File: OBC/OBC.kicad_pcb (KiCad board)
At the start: 4 copper layers, 90.3 x 95.8 mm, 53 parts

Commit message: Clean up GND routing to RPCM4 H1/H2 headers
- Removed 45 degree GND traces running to the H1 and H2 header pads
- Replaced long GND traces with short stubs and vias down to the
  GND plane (layer 2)
- Shorter return paths and less top layer clutter around the headers
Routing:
- net GND: track 225.9 -> 143.6 mm, vias 4 -> 8

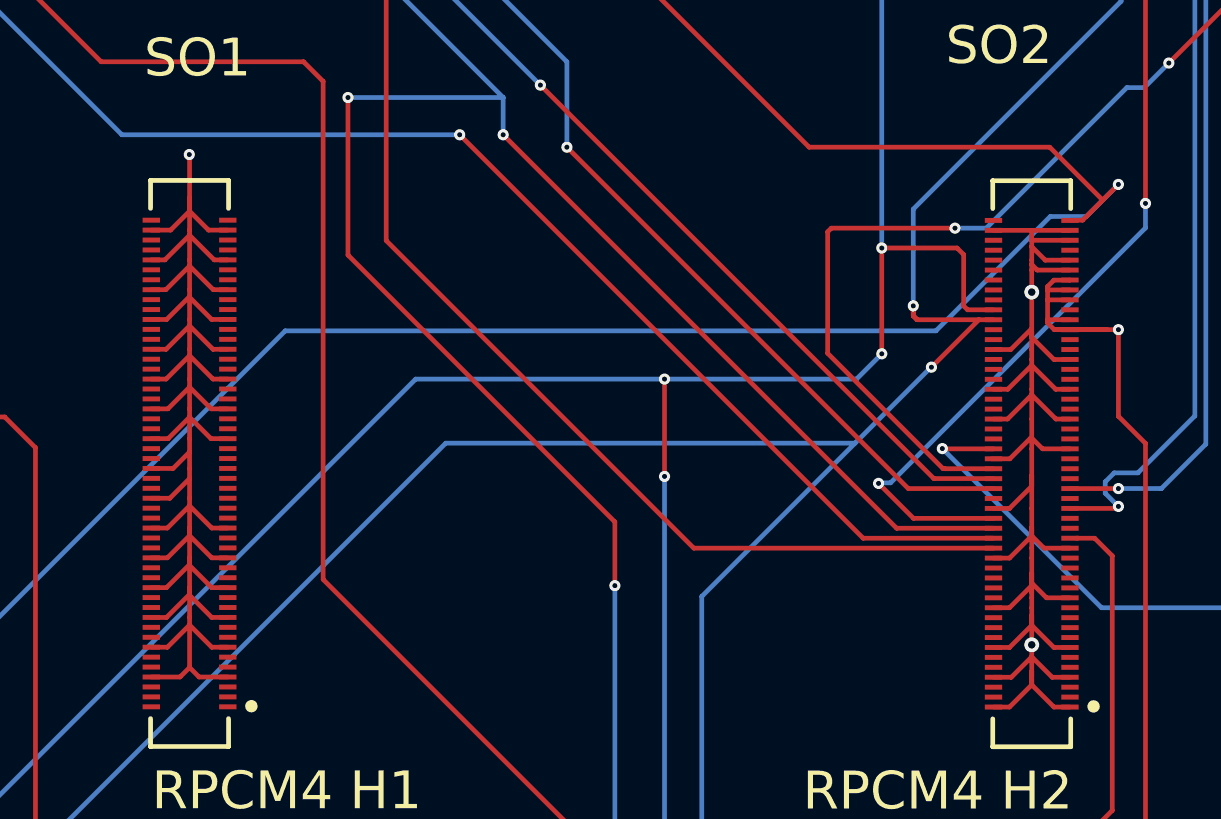
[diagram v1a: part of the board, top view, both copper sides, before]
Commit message: Clean up GND routing on RPCM4 H1 header
- Removed unnecessary long GND traces on H1
- Replaced them with short stubs and vias down to the GND plane
  (layer 2)
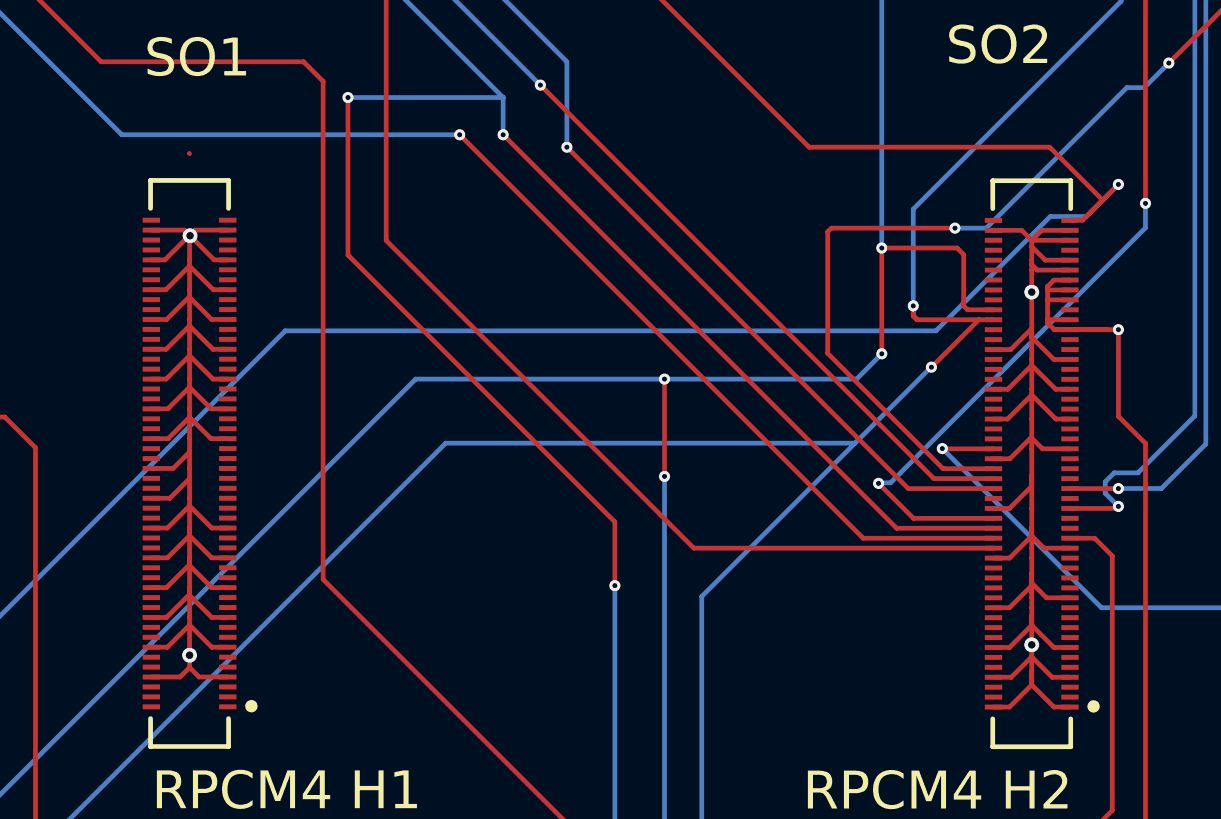
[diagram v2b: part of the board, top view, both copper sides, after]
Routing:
- net GND: track 143.6 -> 139.4 mm, vias 8 -> 9
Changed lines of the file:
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@@
-	)
-	(segment
-		(start 130.51028 89.74366)
-		(end 131.28609 89.74366)
-		(width 0.19)
-		(layer "F.Cu")
-		(net "GND")
 	)
 	(segment
@@
 	)
 	(segment
-		(start 129.74609 88.44947)
-		(end 129.74609 88.82507)
-		(width 0.19)
-		(layer "F.Cu")
-		(net "GND")
-	)
-	(segment
 		(start 164.16011 102.55366)
 		(end 165.20609 102.55366)
@@
 	)
 	(segment
+		(start 164.0661 89.75366)
+		(end 165.20609 89.75366)
+		(width 0.19)
+		(layer "F.Cu")
+		(net "GND")
+	)
+	(segment
 		(start 129.74609 96.06947)
 		(end 129.74609 95.74366)
@@
 	(segment
 		(start 129.74609 89.94947)
-		(end 130.74028 90.94366)
+		(end 129.76679 89.97017)
 		(width 0.19)
 		(layer "F.Cu")
@@
 	)
 	(segment
-		(start 163.6661 90.15366)
-		(end 163.6661 89.75366)
-		(width 0.19)
-		(layer "F.Cu")
-		(net "GND")
-	)
-	(segment
 		(start 163.6661 96.37947)
 		(end 164.64029 97.35366)
@@
 	)
 	(segment
-		(start 129.74609 88.44947)
-		(end 129.74609 86.66427)
-		(width 0.19)
-		(layer "F.Cu")
-		(net "GND")
-	)
-	(segment
 		(start 129.74609 100.84947)
 		(end 128.8519 101.74366)
@@
 	)
 	(segment
+		(start 129.74609 89.94947)
+		(end 129.9519 89.74366)
+		(width 0.19)
+		(layer "F.Cu")
+		(net "GND")
+	)
+	(segment
 		(start 162.69191 97.35366)
 		(end 162.12609 97.35366)
@@
 	)
 	(segment
+		(start 129.74609 89.94947)
+		(end 129.54028 89.74366)
+		(width 0.19)
+		(layer "F.Cu")
+		(net "GND")
+	)
+	(segment
 		(start 129.74609 90.94366)
 		(end 129.74609 89.94947)
@@
 	)
 	(segment
+		(start 163.2661 89.75366)
+		(end 162.12609 89.75366)
+		(width 0.19)
+		(layer "F.Cu")
+		(net "GND")
+	)
+	(segment
 		(start 163.6661 95.18947)
 		(end 163.6661 94.95366)
@@
 	)
 	(segment
-		(start 163.6661 89.75366)
-		(end 162.12609 89.75366)
-		(width 0.19)
-		(layer "F.Cu")
-		(net "GND")
-	)
-	(segment
 		(start 163.6661 93.84947)
 		(end 163.6661 93.70947)
@@
 	)
 	(segment
-		(start 128.9819 89.74366)
-		(end 128.20609 89.74366)
-		(width 0.19)
-		(layer "F.Cu")
-		(net "GND")
-	)
-	(segment
 		(start 129.74609 102.04966)
 		(end 128.85209 102.94366)
@@
 	)
 	(segment
-		(start 129.74609 89.94947)
-		(end 129.74609 89.74366)
-		(width 0.19)
-		(layer "F.Cu")
-		(net "GND")
-	)
-	(segment
 		(start 163.6661 106.92947)
 		(end 163.6661 106.55366)
@@
 	)
 	(segment
-		(start 129.74609 88.97947)
-		(end 130.51028 89.74366)
-		(width 0.19)
-		(layer "F.Cu")
-		(net "GND")
-	)
-	(segment
 		(start 129.74609 97.27947)
 		(end 130.61028 98.14366)
@@
 	)
 	(segment
-		(start 129.74609 88.97947)
-		(end 129.74609 88.44947)
-		(width 0.19)
-		(layer "F.Cu")
-		(net "GND")
-	)
-	(segment
 		(start 129.74609 107.35947)
-		(end 129.74609 105.64966)
+		(end 129.74609 106.86547)
 		(width 0.19)
 		(layer "F.Cu")
@@
 	)
 	(segment
-		(start 129.74609 88.97947)
-		(end 128.9819 89.74366)
+		(start 163.6661 90.15366)
+		(end 164.0661 89.75366)
 		(width 0.19)
 		(layer "F.Cu")
@@
 	)
 	(segment
+		(start 129.54028 89.74366)
+		(end 128.20609 89.74366)
+		(width 0.19)
+		(layer "F.Cu")
+		(net "GND")
+	)
+	(segment
 		(start 129.74609 107.35947)
 		(end 130.13028 107.74366)
@@
 	)
 	(segment
-		(start 163.6661 89.75366)
-		(end 165.20609 89.75366)
-		(width 0.19)
-		(layer "F.Cu")
-		(net "GND")
-	)
-	(segment
 		(start 129.74609 105.64966)
 		(end 128.85209 106.54366)
@@
 	)
 	(segment
+		(start 129.74609 106.86547)
+		(end 129.74609 105.64966)
+		(width 0.19)
+		(layer "F.Cu")
+		(net "GND")
+	)
+	(segment
 		(start 129.74609 92.44966)
 		(end 130.63809 93.34166)
@@
 	)
 	(segment
+		(start 129.76679 89.97017)
+		(end 130.74028 90.94366)
+		(width 0.19)
+		(layer "F.Cu")
+		(net "GND")
+	)
+	(segment
 		(start 163.6661 103.56947)
 		(end 163.6661 102.95366)
@@
 	)
 	(segment
+		(start 129.9519 89.74366)
+		(end 131.28609 89.74366)
+		(width 0.19)
+		(layer "F.Cu")
+		(net "GND")
+	)
+	(segment
 		(start 163.6661 95.18947)
 		(end 164.63029 96.15366)
@@
 	)
 	(segment
-		(start 129.74609 89.74366)
-		(end 129.74609 88.97947)
-		(width 0.19)
-		(layer "F.Cu")
-		(net "GND")
-	)
-	(segment
 		(start 128.85209 102.94366)
 		(end 128.20609 102.94366)
+		(width 0.19)
+		(layer "F.Cu")
+		(net "GND")
+	)
+	(segment
+		(start 163.6661 90.15366)
+		(end 163.2661 89.75366)
 		(width 0.19)
 		(layer "F.Cu")
@@
 	)
 	(via
-		(at 129.73547 86.70066)
-		(size 0.45)
-		(drill 0.2)
-		(layers "F.Cu" "B.Cu")
-		(net "GND")
-	)
-	(via
 		(at 137.81049 137.22867)
 		(size 0.6)
@@
 	)
 	(via
+		(at 129.74609 106.86547)
+		(size 0.6)
+		(drill 0.3)
+		(layers "F.Cu" "B.Cu")
+		(net "GND")
+	)
+	(via
 		(at 177.6786 137.87367)
 		(size 0.6)
@@
 		(size 0.6)
 		(drill 0.3)
+		(layers "F.Cu" "B.Cu")
+		(net "GND")
+	)
+	(via
+		(at 129.76679 89.97017)
+		(size 0.6)
+		(drill 0.3)
